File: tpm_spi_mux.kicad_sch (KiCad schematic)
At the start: 0 parts

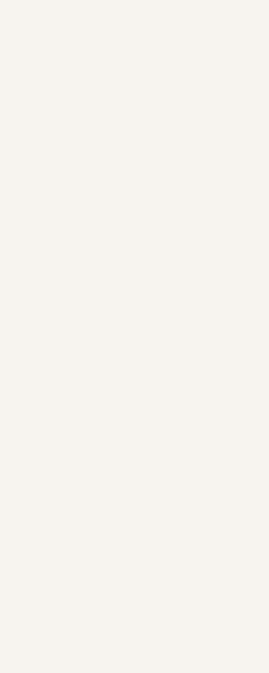
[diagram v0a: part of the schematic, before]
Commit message: [#82233] Add eSPI/QSPI and TPM mux
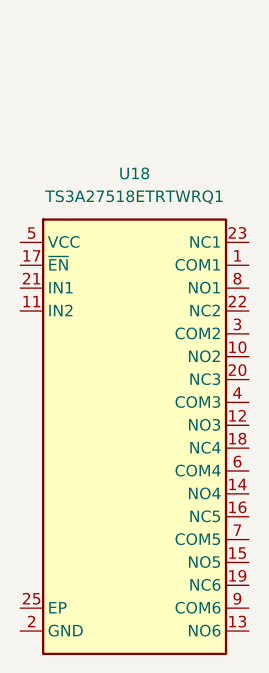
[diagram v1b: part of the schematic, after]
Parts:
- added U18: TS3A27518E_QFN, antmicro-footprints:QFN-24-1EP_4x4mm_P0.5mm_EP2.6x2.6mm, symbol antmicroInterfaceAnalogSwitchesMultiplexersDemultiplexers:TS3A27518E_QFN
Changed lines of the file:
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@@
+		)
+	)
+	(symbol
+		(lib_id "antmicroInterfaceAnalogSwitchesMultiplexersDemultiplexers:TS3A27518E_QFN")
+		(at 163.83 173.99 0)
+		(unit 1)
+		(exclude_from_sim no)
+		(in_bom yes)
+		(on_board yes)
+		(dnp no)
+		(fields_autoplaced yes)
+		(property "Reference" "U18"
+			(at 176.53 166.37 0)
+			(effects
+				(font
+					(size 1.27 1.27)
+					(thickness 0.15)
+				)
+			)
+		)
+		(property "Value" "TS3A27518E_QFN"
+			(at 203.2 179.07 0)
+			(effects
+				(font
+					(size 1.27 1.27)
+					(thickness 0.15)
+				)
+				(justify left bottom)
+				(hide yes)
+			)
+		)
+		(property "Footprint" "antmicro-footprints:QFN-24-1EP_4x4mm_P0.5mm_EP2.6x2.6mm"
+			(at 203.2 181.61 0)
+			(effects
+				(font
+					(size 1.27 1.27)
+					(thickness 0.15)
+				)
+				(justify left bottom)
+				(hide yes)
+			)
+		)
+		(property "Datasheet" "https://www.ti.com/lit/ds/symlink/ts3a27518e-q1.pdf?HQS=dis-mous-null-mousermode-dsf-pf-null-wwe&ts=1685014732392&ref_url=https%253A%252F%252Fwww.mouser.com%252F"
+			(at 203.2 184.15 0)
+			(effects
+				(font
+					(size 1.27 1.27)
+					(thickness 0.15)
+				)
+				(justify left bottom)
+				(hide yes)
+			)
+		)
+		(property "Description" "Interface analog switch/multiplexer/demultiplexer"
+			(at 163.83 173.99 0)
+			(effects
+				(font
+					(size 1.27 1.27)
+				)
+				(hide yes)
+			)
+		)
+		(property "MPN" "TS3A27518ETRTWRQ1"
+			(at 176.53 168.91 0)
+			(effects
+				(font
+					(size 1.27 1.27)
+					(thickness 0.15)
+				)
+			)
+		)
+		(property "Manufacturer" "Texas Instruments"
+			(at 203.2 189.23 0)
+			(effects
+				(font
+					(size 1.27 1.27)
+					(thickness 0.15)
+				)
+				(justify left bottom)
+				(hide yes)
+			)
+		)
+		(property "Author" "Antmicro"
+			(at 203.2 191.77 0)
+			(effects
+				(font
+					(size 1.27 1.27)
+					(thickness 0.15)
+				)
+				(justify left bottom)
+				(hide yes)
+			)
+		)
+		(property "License" "Apache-2.0"
+			(at 203.2 194.31 0)
+			(effects
+				(font
+					(size 1.27 1.27)
+					(thickness 0.15)
+				)
+				(justify left bottom)
+				(hide yes)
+			)
+		)
+		(pin "4"
+		)
+		(pin "1"
+		)
+		(pin "7"
+		)
+		(pin "16"
+		)
+		(pin "24"
+		)
+		(pin "25"
+		)
+		(pin "13"
+		)
+		(pin "9"
+		)
+		(pin "18"
+		)
+		(pin "6"
+		)
+		(pin "8"
+		)
+		(pin "20"
+		)
+		(pin "10"
+		)
+		(pin "23"
+		)
+		(pin "3"
+		)
+		(pin "14"
+		)
+		(pin "12"
+		)
+		(pin "15"
+		)
+		(pin "21"
+		)
+		(pin "11"
+		)
+		(pin "5"
+		)
+		(pin "22"
+		)
+		(pin "2"
+		)
+		(pin "17"
+		)
+		(pin "19"
+		)
+		(instances
+			(project "bmc-reference-carrier-board"
+				(path "/5f636c45-3c15-4731-8931-4625e0dab7e4/e221e630-4eed-4bd7-af61-82caf62956ae"
+					(reference "U18")
+					(unit 1)
+				)
+			)
 		)
 	)

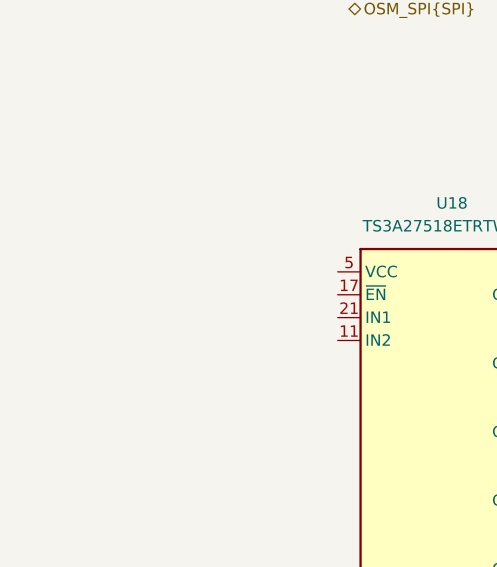
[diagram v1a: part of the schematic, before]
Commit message: [#82323] Connect OSM signals
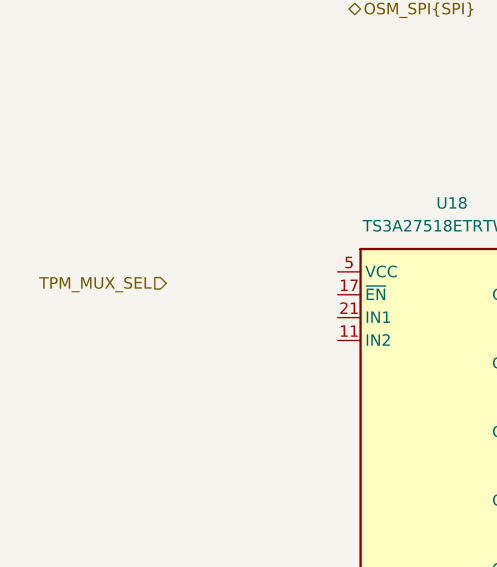
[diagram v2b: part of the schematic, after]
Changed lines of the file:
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@@
+		)
+	)
+	(hierarchical_label "TPM_MUX_SEL"
+		(shape input)
+		(at 144.78 175.26 180)
+		(effects
+			(font
+				(size 1.27 1.27)
+			)
+			(justify right)
 		)
 	)

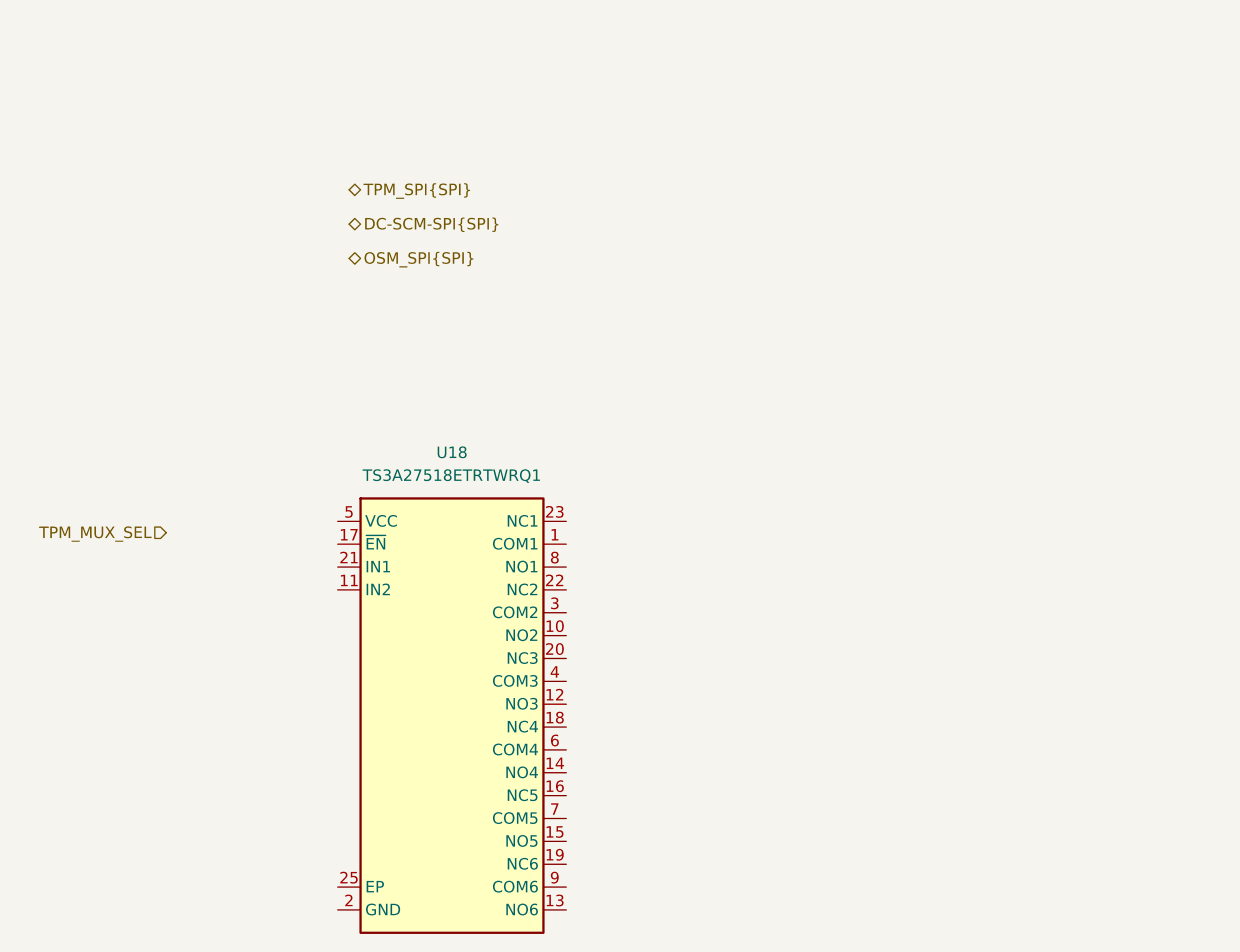
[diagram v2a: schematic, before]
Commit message: [#82233] Added TPM mux
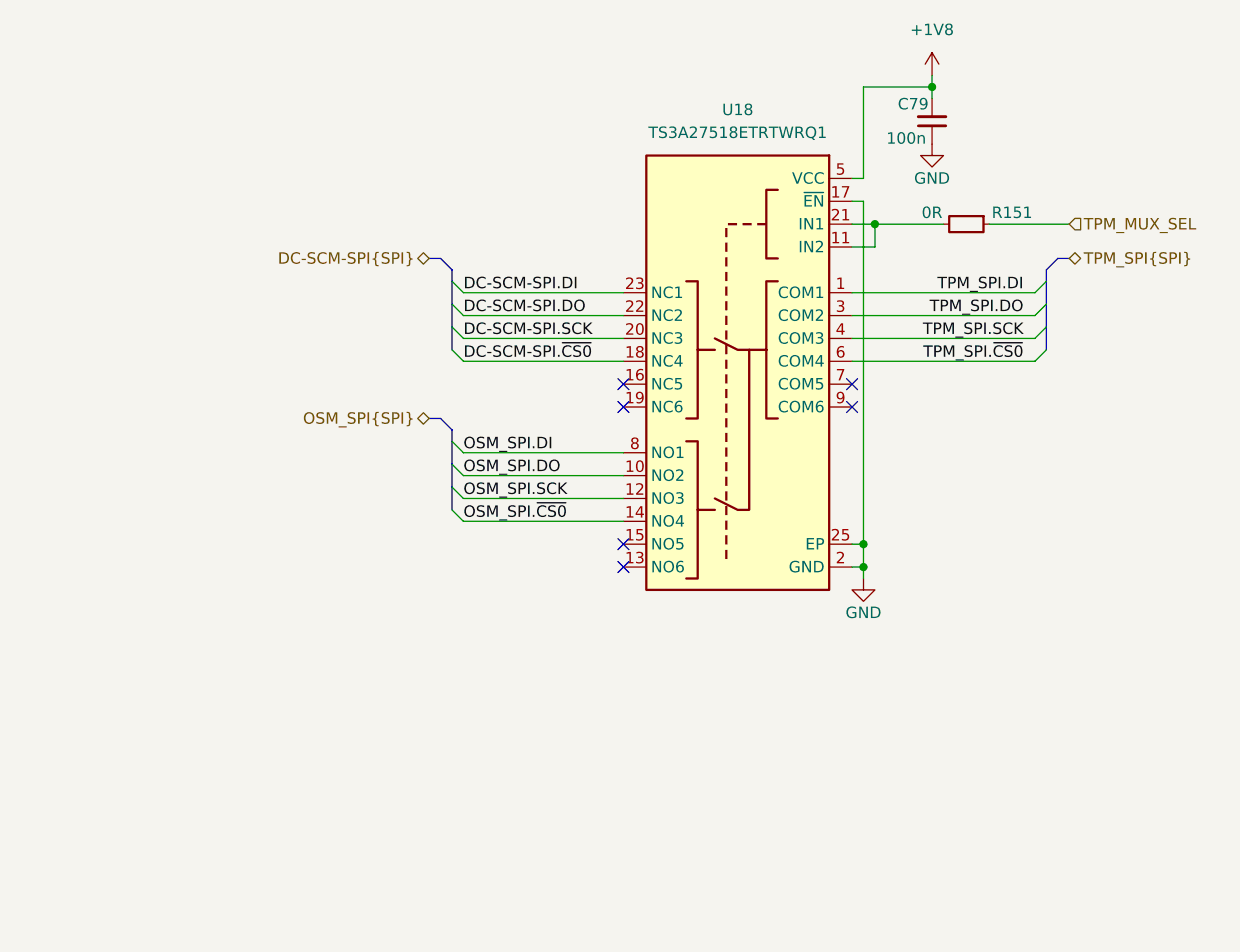
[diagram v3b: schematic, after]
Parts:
- added C79: C_100n_0402, antmicro-footprints:C_0402_1005Metric, symbol antmicroCapacitors0402:C_100n_0402
- added R151: R_0R_0402, antmicro-footprints:R_0402_1005Metric, symbol antmicroResistors0402:R_0R_0402
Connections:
- net TPM_MUX_SEL: now also R151.1
- net TPM_SPI.DI: now reaches U18.1 (COM1)
- net OSM_SPI.DO: now reaches U18.10 (NO2)
- net at U18.11 (IN2): now also U18.21 (IN1), R151.2
- net OSM_SPI.SCK: now reaches U18.12 (NO3)
- net OSM_SPI.~{CS0}: now reaches U18.14 (NO4)
- net GND: now reaches U18.17 (~{EN})
- net GND: now also U18.2 (GND), U18.25 (EP), C79.1
- net DC-SCM-SPI.~{CS0}: now reaches U18.18 (NC4)
- net DC-SCM-SPI.SCK: now reaches U18.20 (NC3)
- net DC-SCM-SPI.DO: now reaches U18.22 (NC2)
- net DC-SCM-SPI.DI: now reaches U18.23 (NC1)
- net TPM_SPI.DO: now reaches U18.3 (COM2)
- net TPM_SPI.SCK: now reaches U18.4 (COM3)
- net +1V8: now reaches U18.5 (VCC)
- net +1V8: now also C79.2
- net TPM_SPI.~{CS0}: now reaches U18.6 (COM4)
- net OSM_SPI.DI: now reaches U18.8 (NO1)
- no-connect marks 0 -> 6

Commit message: [#83609] Reannotate board
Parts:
- renumbered C79 to C53, R151 to R143, U18 to U10
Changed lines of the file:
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@@
 		(on_board yes)
 		(dnp no)
-		(property "Reference" "#PWR0142"
+		(property "Reference" "#PWR099"
 			(at 213.36 182.88 0)
 			(effects
@@
 			(project "bmc-reference-carrier-board"
 				(path "/5f636c45-3c15-4731-8931-4625e0dab7e4/e221e630-4eed-4bd7-af61-82caf62956ae"
-					(reference "#PWR0142")
+					(reference "#PWR099")
 					(unit 1)
 				)
@@
 		(on_board yes)
 		(dnp no)
-		(property "Reference" "#PWR0146"
+		(property "Reference" "#PWR0101"
 			(at 220.98 134.62 0)
 			(effects
@@
 			(project "bmc-reference-carrier-board"
 				(path "/5f636c45-3c15-4731-8931-4625e0dab7e4/e221e630-4eed-4bd7-af61-82caf62956ae"
-					(reference "#PWR0146")
+					(reference "#PWR0101")
 					(unit 1)
 				)
@@
 		(on_board yes)
 		(dnp no)
-		(property "Reference" "C79"
+		(property "Reference" "C53"
 			(at 226.06 127.635 90)
 			(effects
@@
 			(project "bmc-reference-carrier-board"
 				(path "/5f636c45-3c15-4731-8931-4625e0dab7e4/e221e630-4eed-4bd7-af61-82caf62956ae"
-					(reference "C79")
+					(reference "C53")
 					(unit 1)
 				)
@@
 		(on_board yes)
 		(dnp no)
-		(property "Reference" "R151"
+		(property "Reference" "R143"
 			(at 238.76 139.7 0)
 			(effects
@@
 			(project "bmc-reference-carrier-board"
 				(path "/5f636c45-3c15-4731-8931-4625e0dab7e4/e221e630-4eed-4bd7-af61-82caf62956ae"
-					(reference "R151")
+					(reference "R143")
 					(unit 1)
 				)
@@
 		(dnp no)
 		(fields_autoplaced yes)
-		(property "Reference" "#PWR0143"
+		(property "Reference" "#PWR0100"
 			(at 245.11 127 0)
 			(effects
@@
 			(project "bmc-reference-carrier-board"
 				(path "/5f636c45-3c15-4731-8931-4625e0dab7e4/e221e630-4eed-4bd7-af61-82caf62956ae"
-					(reference "#PWR0143")
+					(reference "#PWR0100")
 					(unit 1)
 				)
@@
 		(on_board yes)
 		(dnp no)
-		(property "Reference" "U18"
+		(property "Reference" "U10"
 			(at 208.28 128.27 0)
 			(effects
@@
 			(project "bmc-reference-carrier-board"
 				(path "/5f636c45-3c15-4731-8931-4625e0dab7e4/e221e630-4eed-4bd7-af61-82caf62956ae"
-					(reference "U18")
+					(reference "U10")
 					(unit 1)
 				)

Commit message: [#83736] WIP: Clear ERC
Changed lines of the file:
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@@
 	)
 	(bus_entry
-		(at 176.5358 147.32)
+		(at 175.26 152.4)
+		(size 1.27 1.27)
+		(stroke
+			(width 0)
+			(type default)
+		)
+	)
+	(bus_entry
+		(at 175.26 149.86)
 		(size 1.27 1.27)
 		(stroke
@@
 	)
 	(bus_entry
-		(at 176.5358 152.4)
+		(at 175.26 147.32)
 		(size 1.27 1.27)
 		(stroke
@@
 	)
 	(bus_entry
+		(at 175.26 154.94)
+		(size 1.27 1.27)
+		(stroke
+			(width 0)
+			(type default)
+		)
+	)
+	(bus_entry
 		(at 242.57 154.94)
 		(size -1.27 1.27)
@@
 	)
 	(bus_entry
-		(at 176.5358 154.94)
-		(size 1.27 1.27)
-		(stroke
-			(width 0)
-			(type default)
-		)
-	)
-	(bus_entry
-		(at 176.5358 149.86)
-		(size 1.27 1.27)
-		(stroke
-			(width 0)
-			(type default)
-		)
-	)
-	(bus_entry
 		(at 242.57 152.4)
 		(size -1.27 1.27)
@@
 		)
 	)
-	(bus
-		(pts
-			(xy 176.5358 149.86) (xy 176.5358 152.4)
+	(wire
+		(pts
+			(xy 176.53 153.67) (xy 195.58 153.67)
 		)
 		(stroke
@@
 		)
 	)
-	(bus
-		(pts
-			(xy 176.5358 152.4) (xy 176.5358 154.94)
-		)
-		(stroke
-			(width 0)
-			(type default)
-		)
-	)
 	(wire
 		(pts
@@
 		)
 	)
+	(bus
+		(pts
+			(xy 175.26 147.32) (xy 175.26 149.86)
+		)
+		(stroke
+			(width 0)
+			(type default)
+		)
+	)
 	(wire
 		(pts
@@
 		)
 	)
-	(bus
-		(pts
-			(xy 175.26 144.78) (xy 173.99 144.78)
-		)
-		(stroke
-			(width 0)
-			(type default)
-		)
-	)
 	(wire
 		(pts
@@
 	(bus
 		(pts
+			(xy 172.72 144.78) (xy 173.99 144.78)
+		)
+		(stroke
+			(width 0)
+			(type default)
+		)
+	)
+	(bus
+		(pts
 			(xy 242.57 146.05) (xy 242.57 147.32)
 		)
@@
 	(bus
 		(pts
-			(xy 176.53 146.05) (xy 175.26 144.78)
+			(xy 173.99 144.78) (xy 175.26 146.05)
 		)
 		(stroke
@@
 		)
 	)
+	(wire
+		(pts
+			(xy 176.53 151.13) (xy 195.58 151.13)
+		)
+		(stroke
+			(width 0)
+			(type default)
+		)
+	)
 	(bus
 		(pts
@@
 		)
 	)
+	(bus
+		(pts
+			(xy 175.26 152.4) (xy 175.26 154.94)
+		)
+		(stroke
+			(width 0)
+			(type default)
+		)
+	)
+	(wire
+		(pts
+			(xy 176.53 148.59) (xy 195.58 148.59)
+		)
+		(stroke
+			(width 0)
+			(type default)
+		)
+	)
 	(wire
 		(pts
@@
 	(wire
 		(pts
-			(xy 177.8058 151.13) (xy 195.58 151.13)
-		)
-		(stroke
-			(width 0)
-			(type default)
-		)
-	)
-	(wire
-		(pts
 			(xy 223.52 140.97) (xy 220.98 140.97)
 		)
@@
 	(wire
 		(pts
-			(xy 177.8058 156.21) (xy 195.58 156.21)
-		)
-		(stroke
-			(width 0)
-			(type default)
-		)
-	)
-	(wire
-		(pts
 			(xy 223.52 143.51) (xy 223.52 140.97)
 		)
@@
 		)
 	)
-	(bus
-		(pts
-			(xy 176.5358 146.05) (xy 176.5358 147.32)
-		)
-		(stroke
-			(width 0)
-			(type default)
-		)
-	)
 	(wire
 		(pts
@@
 	(bus
 		(pts
+			(xy 175.26 149.86) (xy 175.26 152.4)
+		)
+		(stroke
+			(width 0)
+			(type default)
+		)
+	)
+	(bus
+		(pts
 			(xy 175.26 162.56) (xy 176.53 163.83)
 		)
@@
 		)
 	)
-	(bus
-		(pts
-			(xy 176.5358 147.32) (xy 176.5358 149.86)
-		)
-		(stroke
-			(width 0)
-			(type default)
-		)
-	)
 	(wire
 		(pts
@@
 	(wire
 		(pts
-			(xy 177.8058 153.67) (xy 195.58 153.67)
-		)
-		(stroke
-			(width 0)
-			(type default)
-		)
-	)
-	(wire
-		(pts
 			(xy 229.87 125.73) (xy 229.87 127)
 		)
@@
 		)
 	)
+	(bus
+		(pts
+			(xy 175.26 146.05) (xy 175.26 147.32)
+		)
+		(stroke
+			(width 0)
+			(type default)
+		)
+	)
 	(wire
 		(pts
@@
 	(wire
 		(pts
-			(xy 177.8058 148.59) (xy 195.58 148.59)
+			(xy 176.53 156.21) (xy 195.58 156.21)
 		)
 		(stroke
@@
 	)
 	(label "DC-SCM-SPI.DI"
-		(at 177.8058 148.59 0)
+		(at 176.53 148.59 0)
 		(effects
 			(font
@@
 	)
 	(label "DC-SCM-SPI.SCK"
-		(at 177.8058 153.67 0)
+		(at 176.53 153.67 0)
 		(effects
 			(font
@@
 	)
 	(label "DC-SCM-SPI.~{CS0}"
-		(at 177.8058 156.21 0)
+		(at 176.53 156.21 0)
 		(effects
 			(font
@@
 	)
 	(label "DC-SCM-SPI.DO"
-		(at 177.8058 151.13 0)
+		(at 176.53 151.13 0)
 		(effects
 			(font
@@
 	(hierarchical_label "DC-SCM-SPI{SPI}"
 		(shape bidirectional)
-		(at 173.99 144.78 180)
-		(effects
-			(font
+		(at 172.72 144.78 180)
+		(effects
+			(font
